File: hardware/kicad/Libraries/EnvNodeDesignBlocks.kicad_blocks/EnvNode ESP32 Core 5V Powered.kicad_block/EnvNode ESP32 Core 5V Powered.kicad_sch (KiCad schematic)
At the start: 2 parts, among them U2 ESP32-DevKitC, U3 24AA025E-OT

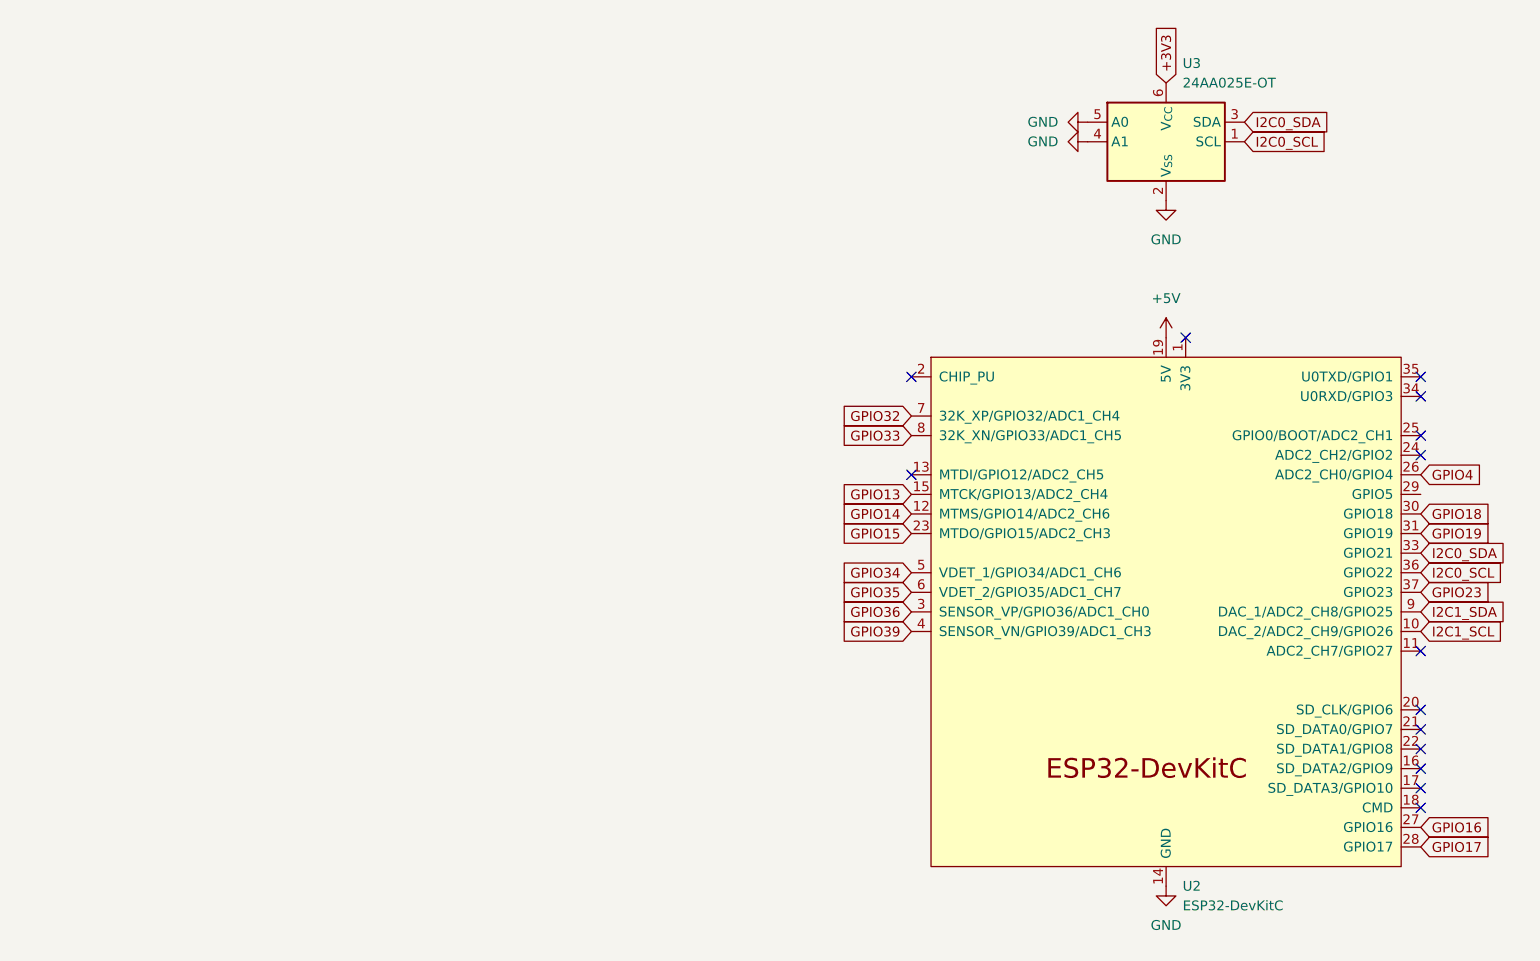
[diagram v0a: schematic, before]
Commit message: DesignBlocks for ESP32 Core
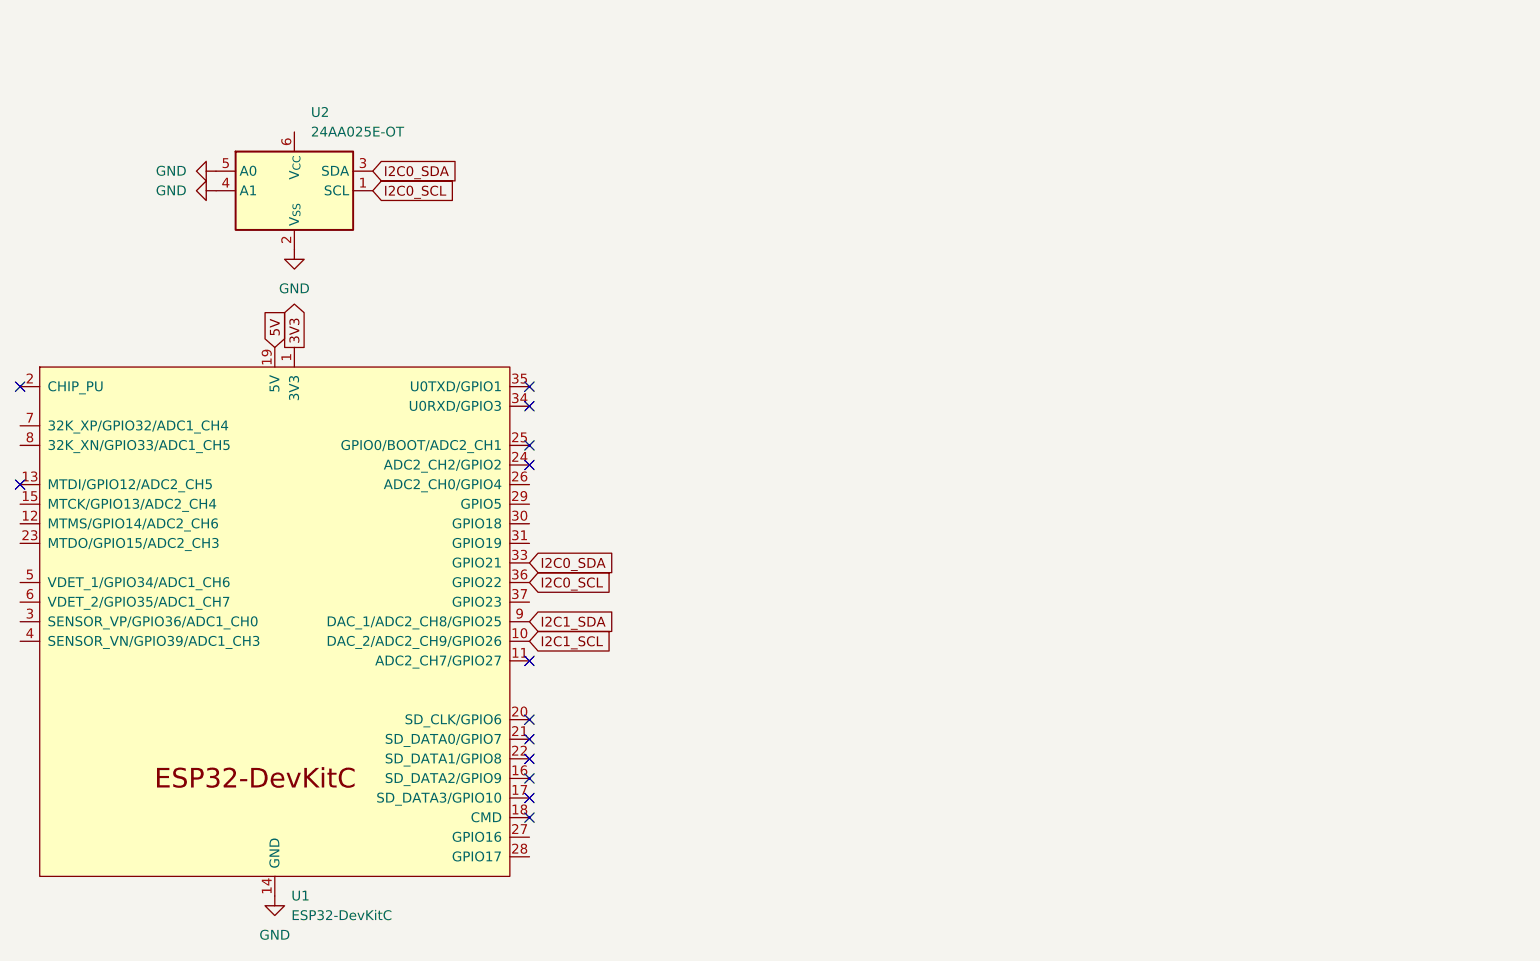
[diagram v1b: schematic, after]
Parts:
- removed U2: ESP32-DevKitC, PCM_Espressif:ESP32-DevKitC, symbol PCM_Espressif:ESP32-DevKitC
- removed U3: 24AA025E-OT, Package_TO_SOT_SMD:SOT-23-6_Handsoldering, symbol Memory_EEPROM:24AA025E-OT
- added U1: ESP32-DevKitC, PCM_Espressif:ESP32-DevKitC, symbol PCM_Espressif:ESP32-DevKitC
- added U2: 24AA025E-OT, Package_TO_SOT_SMD:SOT-23-6, symbol Memory_EEPROM:24AA025E-OT
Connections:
- net GND: now also U1.14 (GND), U1.32 (GND), U1.38 (GND), U2.2 (V_{SS}), U2.4 (A1), U2.5 (A0)
- net I2C0_SCL: now also U1.36 (GPIO22), U2.1 (SCL)
- net I2C0_SDA: now also U1.33 (GPIO21), U2.3 (SDA)
- net I2C1_SCL: now also U1.10 (DAC_2/ADC2_CH9/GPIO26)
- net I2C1_SDA: now also U1.9 (DAC_1/ADC2_CH8/GPIO25)
- new net 3V3: U1.1 (3V3)
- new net 5V: U1.19 (5V)
- no-connect marks 14 -> 13
